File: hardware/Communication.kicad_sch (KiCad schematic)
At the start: 28 parts, among them J17 5-146281-3, J18 Conn_01x04_Pin, J3 USB_C_Receptacle_USB2.0, U21 TXB0102DCUT, U22 ADUM4160

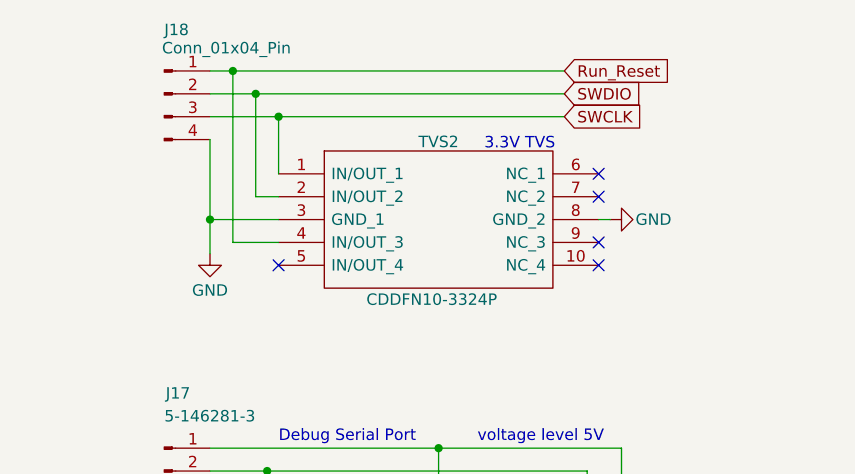
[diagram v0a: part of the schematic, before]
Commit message: draft simplified rp2350 schematic w/sd card
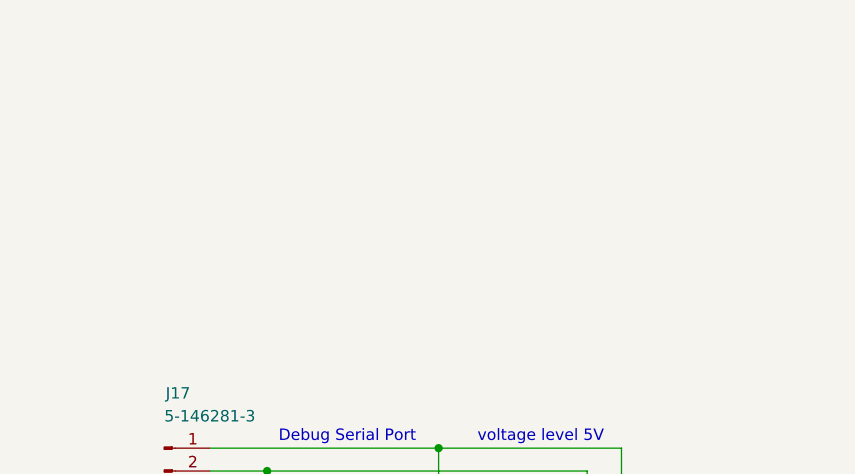
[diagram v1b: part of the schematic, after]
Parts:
- removed J18: Conn_01x04_Pin, Connector_PinHeader_2.54mm:PinHeader_1x04_P2.54mm_Vertical, symbol harp.device.quad.dac:Conn_01x04_Pin
- removed TVS2: CDDFN10-3324P, harp.device.quad.dac.kicad:CDDFN103324P, symbol harp.device.quad.dac:CDDFN10-3324P
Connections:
- no-connect marks 7 -> 2
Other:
- note removed: "3.3V TVS"

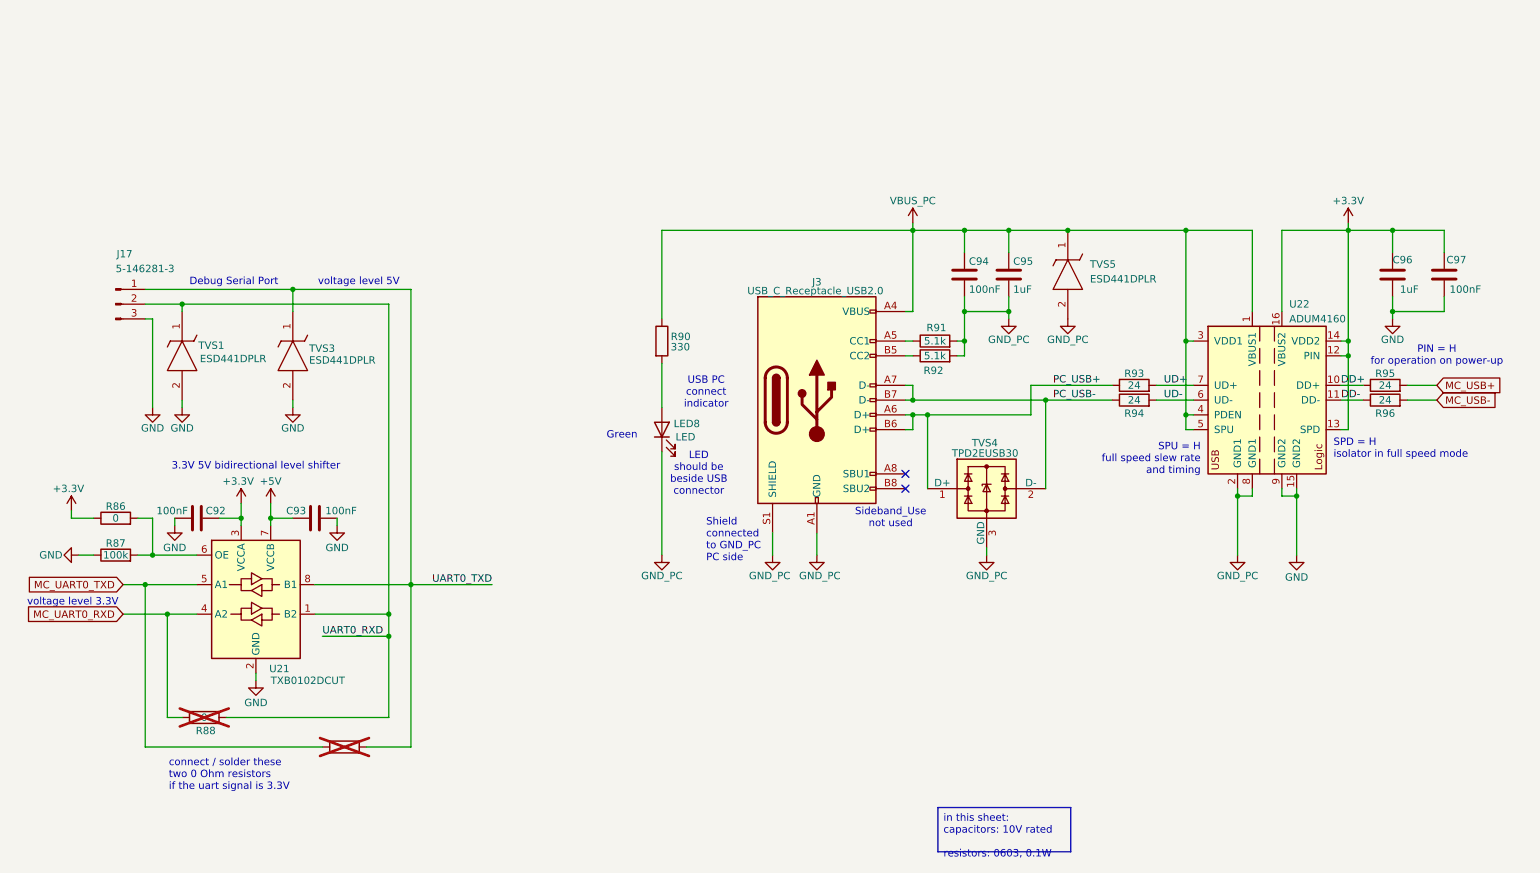
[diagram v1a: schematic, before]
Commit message: draft new analog signal chain & short-circuit detection
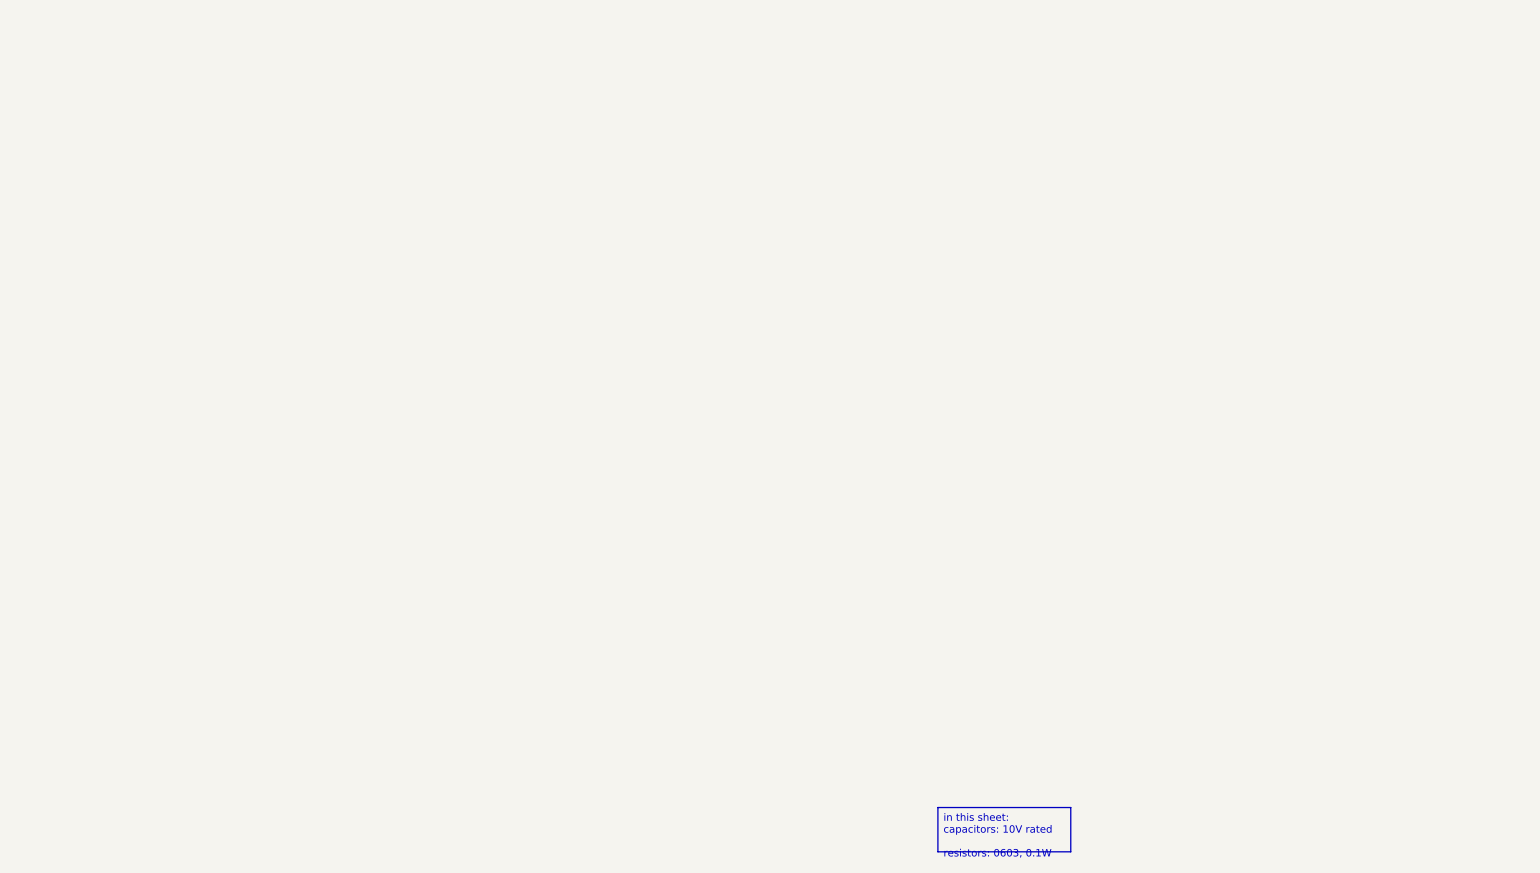
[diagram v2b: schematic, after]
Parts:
- removed C92, C93, C94, C97: 100nF, Capacitor_SMD:C_0603_1608Metric, symbol harp.device.quad.dac:C_0603
- removed C95, C96: 1uF, Capacitor_SMD:C_0603_1608Metric, symbol harp.device.quad.dac:C_0603
- removed J17: 5-146281-3, harp.device.quad.dac.kicad:PinHeader_1x03_P2.54mm_Vertical, symbol harp.device.quad.dac:Conn_01x03_Male
- removed J3: USB_C_Receptacle_USB2.0, harp.device.quad.dac.kicad:USB_C_Receptacle_JAE_DX07S016JA1R1500, symbol harp.device.quad.dac:USB_C_Receptacle_USB2.0
- removed LED8: LED, harp.device.quad.dac.kicad:LED_0603_1608Metric_Pad1.05x0.95mm_HandSolder, symbol harp.device.quad.dac:LED
- removed R86, R88, R89: 0, Resistor_SMD:R_0603_1608Metric, symbol harp.device.quad.dac:R_0603
- removed R87: 100k, Resistor_SMD:R_0603_1608Metric, symbol harp.device.quad.dac:R_0603
- removed R90: 330, Resistor_SMD:R_0603_1608Metric, symbol harp.device.quad.dac:R_0603
- removed R91, R92: 5.1k, Resistor_SMD:R_0603_1608Metric, symbol harp.device.quad.dac:R_0603
- removed R93, R94, R95, R96: 24, Resistor_SMD:R_0603_1608Metric, symbol harp.device.quad.dac:R_0603
- removed TVS1, TVS3, TVS5: ESD441DPLR, harp.device.quad.dac.kicad:ESD441DPLR, symbol harp.device.quad.dac:ESD441DPLR
- removed TVS4: TPD2EUSB30, Package_TO_SOT_SMD:Texas_DRT-3, symbol harp.device.quad.dac:TPD2EUSB30
- removed U21: TXB0102DCUT, harp.device.quad.dac.kicad:SOP50P310X90-8N, symbol harp.device.quad.dac:TXB0102DCT
- removed U22: ADUM4160, harp.device.quad.dac.kicad:SOIC-16W_7.5x10.3mm_P1.27mm, symbol harp.device.quad.dac:ADUM4160
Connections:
- no-connect marks 2 -> 0
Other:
- note removed: "3.3V 5V bidirectional level shifter"
- note removed: "Debug Serial Port"
- note removed: "Green"
- note removed: "LED should be beside USB connector"
- note removed: "PIN = H for operation on power-up"
- note removed: "SPD = H isolator in full speed mode"
- note removed: "SPU = H full speed slew rate and timing"
- note removed: "Shield connected to GND_PC PC side"
- note removed: "Sideband_Use not used"
- note removed: "USB PC connect indicator"
- note removed: "connect / solder these two 0 Ohm resistors if the uart signal is 3.3V"
- note removed: "voltage level 3.3V"
- note removed: "voltage level 5V"
